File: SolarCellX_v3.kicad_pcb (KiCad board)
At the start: 6 copper layers, 48.4 x 48.4 mm, 55 parts, among them J1 XF2M-1015-1A, U2 Value, U3 TSL2561

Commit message: design review and generated gerbers
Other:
- rule pad_to_mask_clearance: 0.0508 -> 0.049
- rule solder_mask_min_width: 0.25 -> 0.099
- board text added: "v02"
- board text removed: "v01"

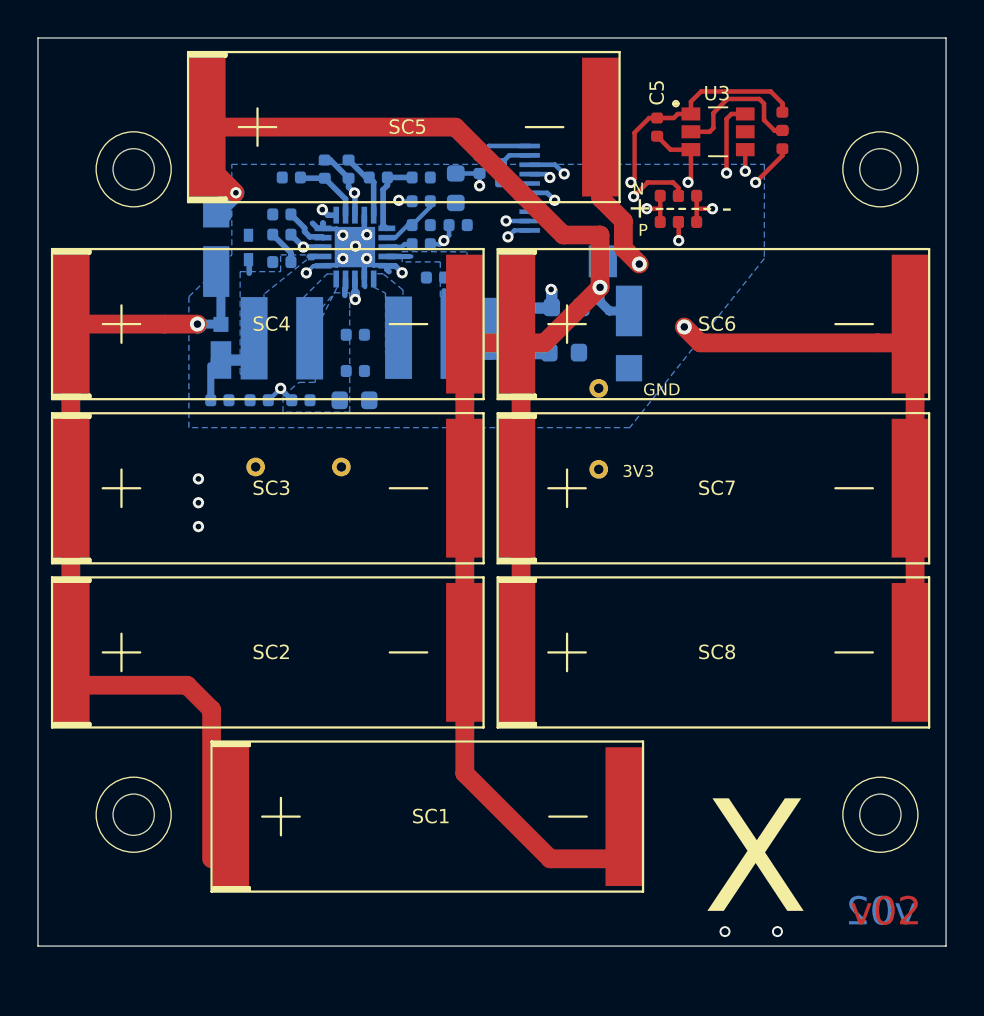
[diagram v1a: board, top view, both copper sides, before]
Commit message: added fiducials, regenerated 3d model and gerbers
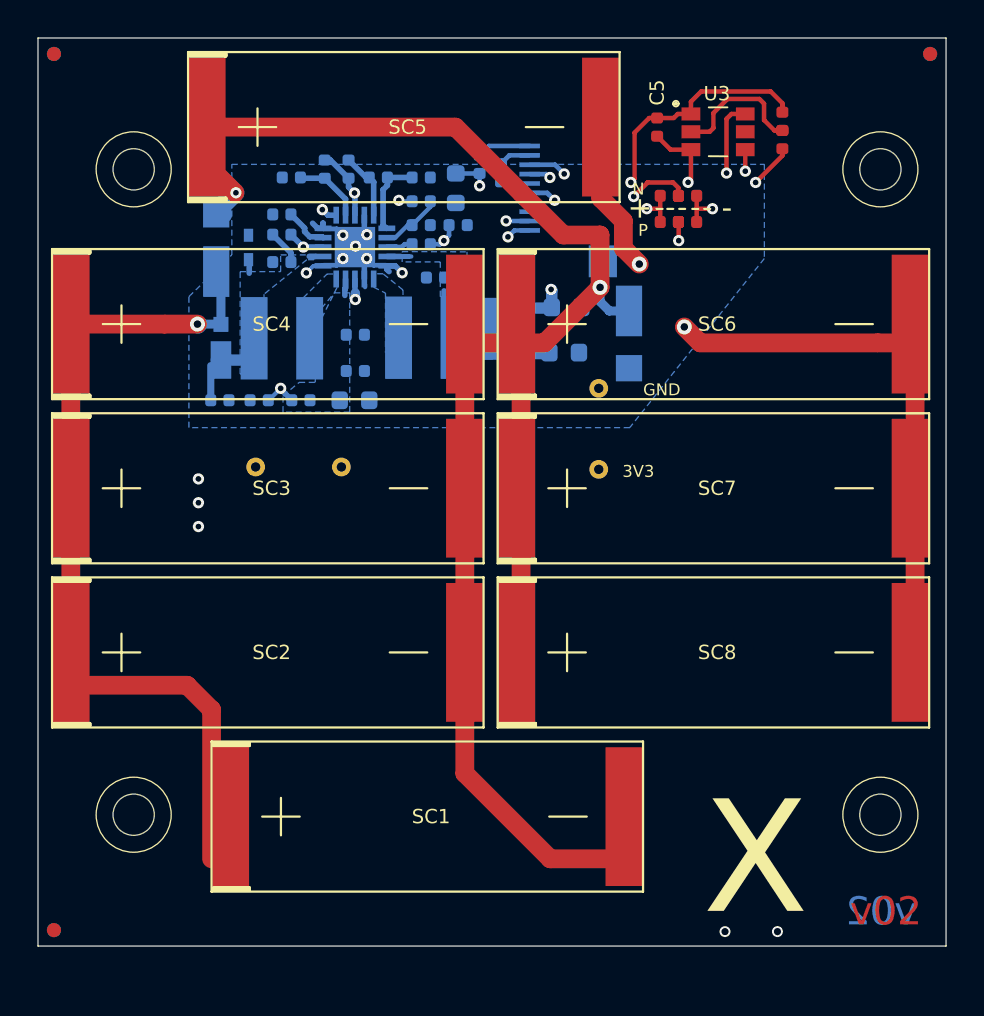
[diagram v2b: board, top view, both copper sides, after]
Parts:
- added REF**: Fiducial_0.75mm_Mask1.5mm, Fiducial:Fiducial_0.75mm_Mask1.5mm, B.Cu at (90.8, 87.5)
- added REF**: Fiducial_0.75mm_Mask1.5mm, Fiducial:Fiducial_0.75mm_Mask1.5mm, B.Cu at (90.8, 40.9)
- added REF**: Fiducial_0.75mm_Mask1.5mm, Fiducial:Fiducial_0.75mm_Mask1.5mm, B.Cu at (137.6, 40.9)
- added REF**: Fiducial_0.75mm_Mask1.5mm, Fiducial:Fiducial_0.75mm_Mask1.5mm, F.Cu at (137.6, 40.9)
- added REF**: Fiducial_0.75mm_Mask1.5mm, Fiducial:Fiducial_0.75mm_Mask1.5mm, F.Cu at (90.8, 40.9)
- added REF**: Fiducial_0.75mm_Mask1.5mm, Fiducial:Fiducial_0.75mm_Mask1.5mm, F.Cu at (90.8, 87.5)
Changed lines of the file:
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@@
     (tracks 1563)
     (zones 0)
-    (modules 55)
+    (modules 61)
     (nets 28)
   )
@@
   (layers
     (0 Top signal)
-    (1 In1.Cu signal)
-    (2 In2.Cu signal)
-    (3 In3.Cu signal)
-    (4 In4.Cu signal)
+    (1 In1.Cu signal hide)
+    (2 In2.Cu signal hide)
+    (3 In3.Cu signal hide)
+    (4 In4.Cu signal hide)
     (31 Bottom signal)
     (32 B.Adhes user hide)
@@
     (35 F.Paste user hide)
     (36 B.SilkS user)
-    (37 F.SilkS user hide)
+    (37 F.SilkS user)
     (38 B.Mask user)
     (39 F.Mask user)
@@
     (add_net VSOLAR)
   )
+  (module Fiducial:Fiducial_0.75mm_Mask1.5mm (layer Bottom)
+    (at 90.85 87.55)
+    (descr "Circular Fiducial, 0.75mm bare copper, 1.5mm soldermask opening (Level B)")
+    (tags fiducial)
+    (attr smd)
+    (fp_text reference REF** (at 0 2) (layer B.SilkS) hide
+      (effects (font (size 1 1) (thickness 0.15)) (justify mirror))
+    )
+    (fp_text value Fiducial_0.75mm_Mask1.5mm (at 0 -2) (layer B.Fab)
+      (effects (font (size 1 1) (thickness 0.15)) (justify mirror))
+    )
+    (fp_circle (center 0 0) (end 1 0) (layer B.CrtYd) (width 0.05))
+    (fp_text user %R (at 0 0) (layer B.Fab)
+      (effects (font (size 0.3 0.3) (thickness 0.05)) (justify mirror))
+    )
+    (fp_circle (center 0 0) (end 0.75 0) (layer B.Fab) (width 0.1))
+    (pad "" smd circle (at 0 0) (size 0.75 0.75) (layers Bottom B.Mask)
+      (solder_mask_margin 0.375) (clearance 0.375))
+  )
+  (module Fiducial:Fiducial_0.75mm_Mask1.5mm (layer Bottom)
+    (at 90.85 40.85)
+    (descr "Circular Fiducial, 0.75mm bare copper, 1.5mm soldermask opening (Level B)")
+    (tags fiducial)
+    (attr smd)
+    (fp_text reference REF** (at 0 2) (layer B.SilkS) hide
+      (effects (font (size 1 1) (thickness 0.15)) (justify mirror))
+    )
+    (fp_text value Fiducial_0.75mm_Mask1.5mm (at 0 -2) (layer B.Fab)
+      (effects (font (size 1 1) (thickness 0.15)) (justify mirror))
+    )
+    (fp_circle (center 0 0) (end 1 0) (layer B.CrtYd) (width 0.05))
+    (fp_text user %R (at 0 0) (layer B.Fab)
+      (effects (font (size 0.3 0.3) (thickness 0.05)) (justify mirror))
+    )
+    (fp_circle (center 0 0) (end 0.75 0) (layer B.Fab) (width 0.1))
+    (pad "" smd circle (at 0 0) (size 0.75 0.75) (layers Bottom B.Mask)
+      (solder_mask_margin 0.375) (clearance 0.375))
+  )
+  (module Fiducial:Fiducial_0.75mm_Mask1.5mm (layer Bottom)
+    (at 137.55 40.85)
+    (descr "Circular Fiducial, 0.75mm bare copper, 1.5mm soldermask opening (Level B)")
+    (tags fiducial)
+    (attr smd)
+    (fp_text reference REF** (at 0 2) (layer B.SilkS) hide
+      (effects (font (size 1 1) (thickness 0.15)) (justify mirror))
+    )
+    (fp_text value Fiducial_0.75mm_Mask1.5mm (at 0 -2) (layer B.Fab)
+      (effects (font (size 1 1) (thickness 0.15)) (justify mirror))
+    )
+    (fp_circle (center 0 0) (end 0.75 0) (layer B.Fab) (width 0.1))
+    (fp_text user %R (at 0 0) (layer B.Fab)
+      (effects (font (size 0.3 0.3) (thickness 0.05)) (justify mirror))
+    )
+    (fp_circle (center 0 0) (end 1 0) (layer B.CrtYd) (width 0.05))
+    (pad "" smd circle (at 0 0) (size 0.75 0.75) (layers Bottom B.Mask)
+      (solder_mask_margin 0.375) (clearance 0.375))
+  )
+  (module Fiducial:Fiducial_0.75mm_Mask1.5mm (layer Top)
+    (at 137.55 40.85)
+    (descr "Circular Fiducial, 0.75mm bare copper, 1.5mm soldermask opening (Level B)")
+    (tags fiducial)
+    (attr smd)
+    (fp_text reference REF** (at 0 -2) (layer F.SilkS) hide
+      (effects (font (size 1 1) (thickness 0.15)))
+    )
+    (fp_text value Fiducial_0.75mm_Mask1.5mm (at 0 2) (layer F.Fab)
+      (effects (font (size 1 1) (thickness 0.15)))
+    )
+    (fp_circle (center 0 0) (end 1 0) (layer F.CrtYd) (width 0.05))
+    (fp_text user %R (at 0 0) (layer F.Fab)
+      (effects (font (size 0.3 0.3) (thickness 0.05)))
+    )
+    (fp_circle (center 0 0) (end 0.75 0) (layer F.Fab) (width 0.1))
+    (pad "" smd circle (at 0 0) (size 0.75 0.75) (layers Top F.Mask)
+      (solder_mask_margin 0.375) (clearance 0.375))
+  )
+  (module Fiducial:Fiducial_0.75mm_Mask1.5mm (layer Top)
+    (at 90.85 40.85)
+    (descr "Circular Fiducial, 0.75mm bare copper, 1.5mm soldermask opening (Level B)")
+    (tags fiducial)
+    (attr smd)
+    (fp_text reference REF** (at 0 -2) (layer F.SilkS) hide
+      (effects (font (size 1 1) (thickness 0.15)))
+    )
+    (fp_text value Fiducial_0.75mm_Mask1.5mm (at 0 2) (layer F.Fab)
+      (effects (font (size 1 1) (thickness 0.15)))
+    )
+    (fp_circle (center 0 0) (end 0.75 0) (layer F.Fab) (width 0.1))
+    (fp_text user %R (at 0 0) (layer F.Fab)
+      (effects (font (size 0.3 0.3) (thickness 0.05)))
+    )
+    (fp_circle (center 0 0) (end 1 0) (layer F.CrtYd) (width 0.05))
+    (pad "" smd circle (at 0 0) (size 0.75 0.75) (layers Top F.Mask)
+      (solder_mask_margin 0.375) (clearance 0.375))
+  )
   (module custom-footprints:KXOB25-05X3F (layer Top)
     (at 100.25 81.5)
@@
     )
   )
+  (module Fiducial:Fiducial_0.75mm_Mask1.5mm (layer Top)
+    (at 90.85 87.55)
+    (descr "Circular Fiducial, 0.75mm bare copper, 1.5mm soldermask opening (Level B)")
+    (tags fiducial)
+    (attr smd)
+    (fp_text reference REF** (at 0 -2) (layer F.SilkS) hide
+      (effects (font (size 1 1) (thickness 0.15)))
+    )
+    (fp_text value Fiducial_0.75mm_Mask1.5mm (at 0 2) (layer F.Fab)
+      (effects (font (size 1 1) (thickness 0.15)))
+    )
+    (fp_circle (center 0 0) (end 1 0) (layer F.CrtYd) (width 0.05))
+    (fp_text user %R (at 0 0) (layer F.Fab)
+      (effects (font (size 0.3 0.3) (thickness 0.05)))
+    )
+    (fp_circle (center 0 0) (end 0.75 0) (layer F.Fab) (width 0.1))
+    (pad "" smd circle (at 0 0) (size 0.75 0.75) (layers Top F.Mask)
+      (solder_mask_margin 0.375) (clearance 0.375))
+  )
   (gr_text X (at 128.25 83.75) (layer F.SilkS)
